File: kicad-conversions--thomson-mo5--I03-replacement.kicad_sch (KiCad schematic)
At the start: 3 parts, among them U1 HM7603_32×8_PROM_THREE-STATE_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, U2 HIGH_PERFORMANCE_E2_CMOS_PLD_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

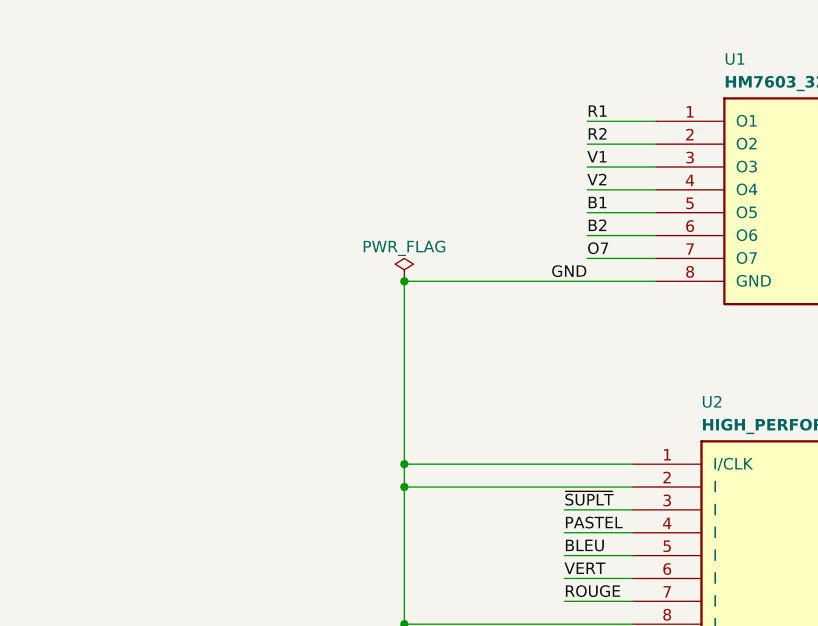
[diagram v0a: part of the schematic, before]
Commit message: Resolves #6 : Add a breakout connector with R[1..2], V[1..2] and B[1..2] for adding custom DAC mods
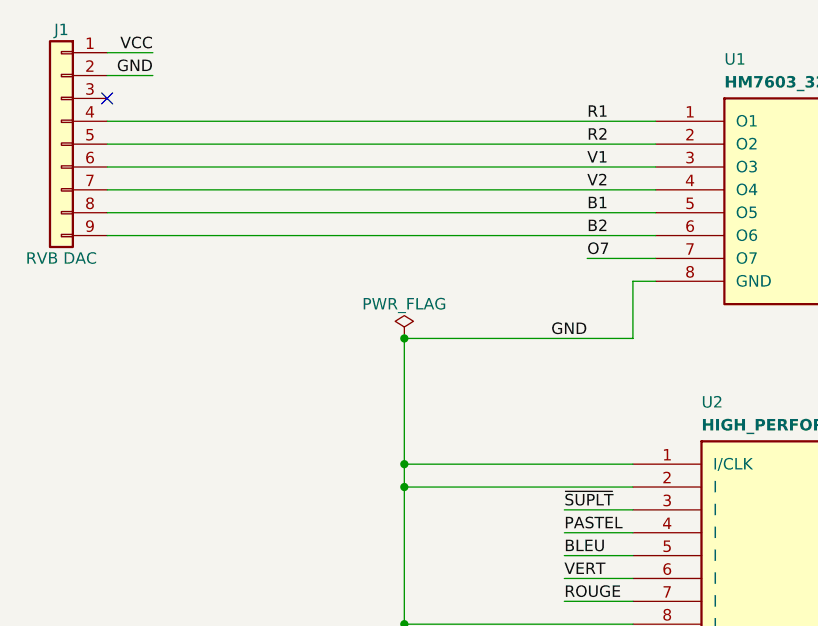
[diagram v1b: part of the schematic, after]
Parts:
- added J1: RVB DAC, Connector_PinHeader_2.54mm:PinHeader_1x09_P2.54mm_Vertical, symbol Connector_Generic:Conn_01x09
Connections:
- net B1: now also J1.8 (Pin_8)
- net B2: now also J1.9 (Pin_9)
- net GND: now also J1.2 (Pin_2)
- net R1: now also J1.4 (Pin_4)
- net R2: now also J1.5 (Pin_5)
- net V1: now also J1.6 (Pin_6)
- net V2: now also J1.7 (Pin_7)
- net VCC: now also J1.1 (Pin_1)
- no-connect marks 0 -> 1
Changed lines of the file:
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@@
   (title_block
     (title "Replacement of I03 (color PROM) for the Thomson MO5")
-    (date "2025-01-25")
-    (rev "v1.0.0")
+    (date "2025-07-27")
+    (rev "v2.0.0")
     (company "Sporniket")
     (comment 3 "https://github.com/sporniket/kicad-conversions--thomson-mo5--i03-replacement")
@@
   (junction (at 63.5 149.86) (diameter 0) (color 0 0 0 0)
   )
-  (junction (at 63.5 106.68) (diameter 0) (color 0 0 0 0)
-  )
   (junction (at 165.1 88.9) (diameter 0) (color 0 0 0 0)
   )
@@
   (junction (at 165.1 127) (diameter 0) (color 0 0 0 0)
   )
+  (junction (at 63.5 113.03) (diameter 0) (color 0 0 0 0)
+  )
+  (no_connect (at 30.48 86.36))
   (wire (pts (xy 63.5 127) (xy 88.9 127))
     (stroke (width 0) (type default))
   )
-  (wire (pts (xy 63.5 106.68) (xy 63.5 127))
-    (stroke (width 0) (type default))
-  )
   (wire (pts (xy 63.5 129.54) (xy 63.5 144.78))
     (stroke (width 0) (type default))
@@
     (stroke (width 0) (type default))
   )
+  (wire (pts (xy 30.48 81.28) (xy 35.56 81.28))
+    (stroke (width 0) (type default))
+  )
+  (wire (pts (xy 30.48 91.44) (xy 91.44 91.44))
+    (stroke (width 0) (type default))
+  )
+  (wire (pts (xy 30.48 93.98) (xy 91.44 93.98))
+    (stroke (width 0) (type default))
+  )
   (wire (pts (xy 81.28 134.62) (xy 88.9 134.62))
     (stroke (width 0) (type default))
@@
     (stroke (width 0) (type default))
   )
-  (wire (pts (xy 83.82 93.98) (xy 91.44 93.98))
+  (wire (pts (xy 30.48 88.9) (xy 91.44 88.9))
     (stroke (width 0) (type default))
   )
@@
     (stroke (width 0) (type default))
   )
-  (wire (pts (xy 83.82 99.06) (xy 91.44 99.06))
-    (stroke (width 0) (type default))
-  )
   (wire (pts (xy 63.5 144.78) (xy 88.9 144.78))
     (stroke (width 0) (type default))
   )
+  (wire (pts (xy 30.48 96.52) (xy 91.44 96.52))
+    (stroke (width 0) (type default))
+  )
   (wire (pts (xy 127 132.08) (xy 134.62 132.08))
     (stroke (width 0) (type default))
@@
     (stroke (width 0) (type default))
   )
+  (wire (pts (xy 30.48 99.06) (xy 91.44 99.06))
+    (stroke (width 0) (type default))
+  )
   (wire (pts (xy 63.5 158.75) (xy 165.1 158.75))
     (stroke (width 0) (type default))
@@
     (stroke (width 0) (type default))
   )
-  (wire (pts (xy 83.82 101.6) (xy 91.44 101.6))
-    (stroke (width 0) (type default))
-  )
   (wire (pts (xy 63.5 147.32) (xy 63.5 149.86))
     (stroke (width 0) (type default))
@@
     (stroke (width 0) (type default))
   )
+  (wire (pts (xy 30.48 101.6) (xy 91.44 101.6))
+    (stroke (width 0) (type default))
+  )
   (wire (pts (xy 124.46 106.68) (xy 132.08 106.68))
     (stroke (width 0) (type default))
@@
     (stroke (width 0) (type default))
   )
-  (wire (pts (xy 83.82 96.52) (xy 91.44 96.52))
-    (stroke (width 0) (type default))
-  )
   (wire (pts (xy 124.46 91.44) (xy 132.08 91.44))
     (stroke (width 0) (type default))
@@
     (stroke (width 0) (type default))
   )
+  (wire (pts (xy 63.5 113.03) (xy 63.5 127))
+    (stroke (width 0) (type default))
+  )
+  (wire (pts (xy 88.9 113.03) (xy 88.9 106.68))
+    (stroke (width 0) (type default))
+  )
   (wire (pts (xy 127 144.78) (xy 134.62 144.78))
     (stroke (width 0) (type default))
   )
-  (wire (pts (xy 91.44 106.68) (xy 63.5 106.68))
+  (wire (pts (xy 88.9 113.03) (xy 63.5 113.03))
     (stroke (width 0) (type default))
   )
@@
     (stroke (width 0) (type default))
   )
-  (wire (pts (xy 83.82 88.9) (xy 91.44 88.9))
-    (stroke (width 0) (type default))
-  )
   (wire (pts (xy 127 137.16) (xy 134.62 137.16))
     (stroke (width 0) (type default))
@@
     (stroke (width 0) (type default))
   )
-  (wire (pts (xy 83.82 91.44) (xy 91.44 91.44))
-    (stroke (width 0) (type default))
-  )
   (wire (pts (xy 124.46 99.06) (xy 132.08 99.06))
     (stroke (width 0) (type default))
@@
     (stroke (width 0) (type default))
   )
+  (wire (pts (xy 30.48 83.82) (xy 35.56 83.82))
+    (stroke (width 0) (type default))
+  )
+  (wire (pts (xy 88.9 106.68) (xy 91.44 106.68))
+    (stroke (width 0) (type default))
+  )
   (text "Récupérer C22 de\nla carte-mère et\nle placer en C1" (at 166.37 135.89 0)
     (effects (font (size 1.27 1.27)) (justify left bottom))
@@
     (effects (font (size 1.27 1.27)) (justify left bottom))
   )
-  (label "GND" (at 83.82 106.68 180) (fields_autoplaced)
+  (label "GND" (at 83.82 113.03 180) (fields_autoplaced)
     (effects (font (size 1.27 1.27)) (justify right bottom))
   )
@@
     (effects (font (size 1.27 1.27)) (justify right bottom))
   )
+  (label "GND" (at 35.56 83.82 180) (fields_autoplaced)
+    (effects (font (size 1.27 1.27)) (justify right bottom))
+  )
   (label "BLEU" (at 132.08 99.06 180) (fields_autoplaced)
     (effects (font (size 1.27 1.27)) (justify right bottom))
@@
   (label "V1" (at 83.82 93.98 0) (fields_autoplaced)
     (effects (font (size 1.27 1.27)) (justify left bottom))
+  )
+  (label "VCC" (at 35.56 81.28 180) (fields_autoplaced)
+    (effects (font (size 1.27 1.27)) (justify right bottom))
   )
   (label "VERT" (at 81.28 139.7 0) (fields_autoplaced)
@@
     )
   )
-  (symbol (lib_id "power:PWR_FLAG") (at 63.5 106.68 0) (unit 1)
-    (in_bom yes) (on_board yes) (dnp no)
-    (property "Reference" "#FLG02" (at 63.5 104.775 0)
-      (effects (font (size 1.27 1.27)) hide)
-    )
-    (property "Value" "PWR_FLAG" (at 63.5 102.87 0)
+  (symbol (lib_id "power:PWR_FLAG") (at 63.5 113.03 0) (unit 1)
+    (in_bom yes) (on_board yes) (dnp no)
+    (property "Reference" "#FLG02" (at 63.5 111.125 0)
+      (effects (font (size 1.27 1.27)) hide)
+    )
+    (property "Value" "PWR_FLAG" (at 63.5 109.22 0)
       (effects (font (size 1.27 1.27)))
     )
-    (property "Footprint" "" (at 63.5 106.68 0)
-      (effects (font (size 1.27 1.27)) hide)
-    )
-    (property "Datasheet" "~" (at 63.5 106.68 0)
+    (property "Footprint" "" (at 63.5 113.03 0)
+      (effects (font (size 1.27 1.27)) hide)
+    )
+    (property "Datasheet" "~" (at 63.5 113.03 0)
       (effects (font (size 1.27 1.27)) hide)
     )
@@
         )
       )
+    )
+  )
+  (symbol (lib_id "Connector_Generic:Conn_01x09") (at 25.4 91.44 0) (mirror y) (unit 1)
+    (in_bom yes) (on_board yes) (dnp no)
+    (property "Reference" "J1" (at 25.4 78.74 0)
+      (effects (font (size 1.27 1.27)))
+    )
+    (property "Value" "RVB DAC" (at 25.4 104.14 0)
+      (effects (font (size 1.27 1.27)))
+    )
+    (property "Footprint" "Connector_PinHeader_2.54mm:PinHeader_1x09_P2.54mm_Vertical" (at 25.4 91.44 0)
+      (effects (font (size 1.27 1.27)) hide)
+    )
+    (property "Datasheet" "~" (at 25.4 91.44 0)
+      (effects (font (size 1.27 1.27)) hide)
+    )
+    (pin "4")
+    (pin "1")
+    (pin "2")
+    (pin "7")
+    (pin "6")
+    (pin "5")
+    (pin "8")
+    (pin "3")
+    (pin "9")
+    (instances
+      (project "kicad-conversions--thomson-mo5--I03-replacement"
+        (path "/65ee49be-62d8-4bd4-a7c2-5144822a98e0"
+          (reference "J1") (unit 1)
+        )
+      )
